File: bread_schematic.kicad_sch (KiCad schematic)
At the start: 1 part, among them U1 NHD-C0220BIZ

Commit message: xganges
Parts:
- removed U1: NHD-C0220BIZ, Display:NHD-C0220BiZ, symbol Display_Character:NHD-C0220BIZ
- added J1: Conn_01x04_Pin, symbol Connector:Conn_01x04_Pin
- added M1: ~, symbol _custom:NUCLEO_G031K8_CN3
- added M2: ~, symbol _custom:NUCLEO-G031K8_CN4
- added U2: TCS34725, TCS34725FN:SON65P200X240X70-6N, symbol TCS34725FN:TCS34725FN

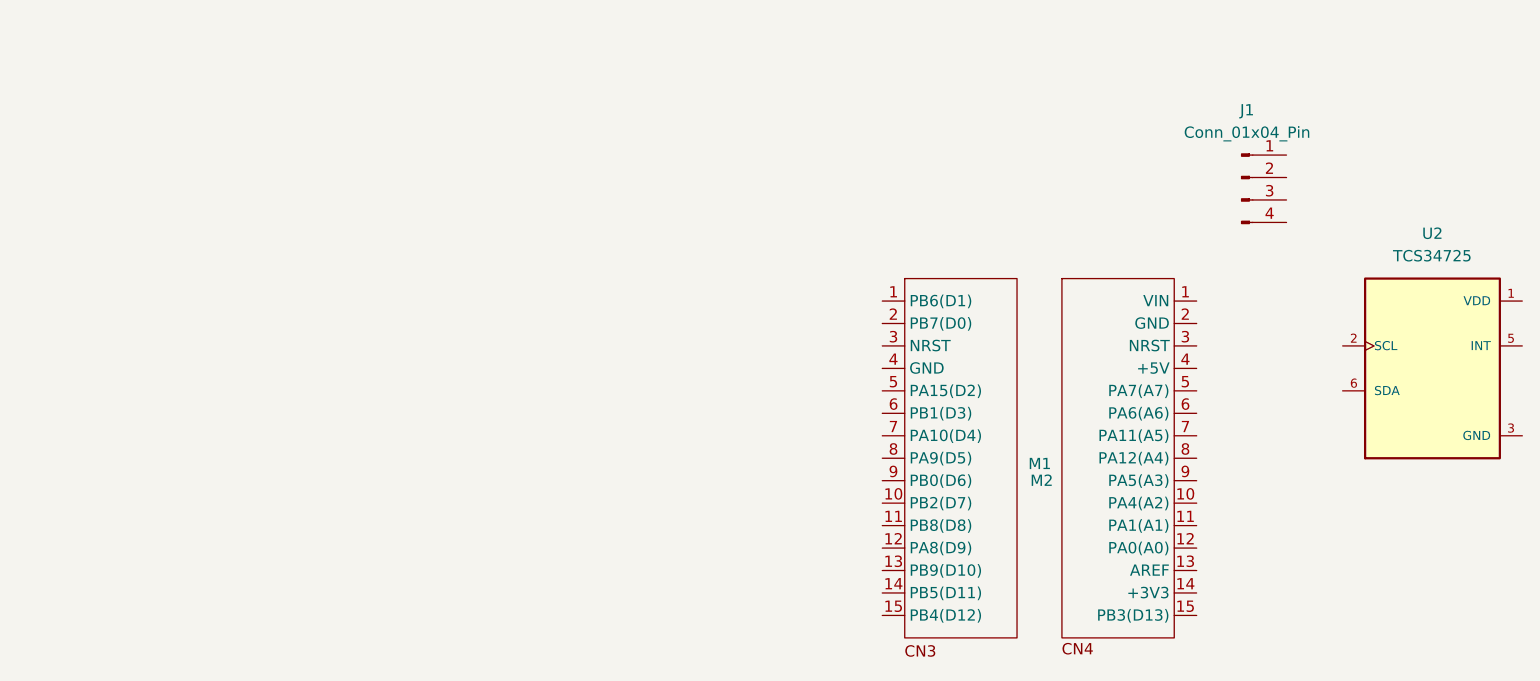
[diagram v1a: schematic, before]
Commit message: finished breadboard schematic
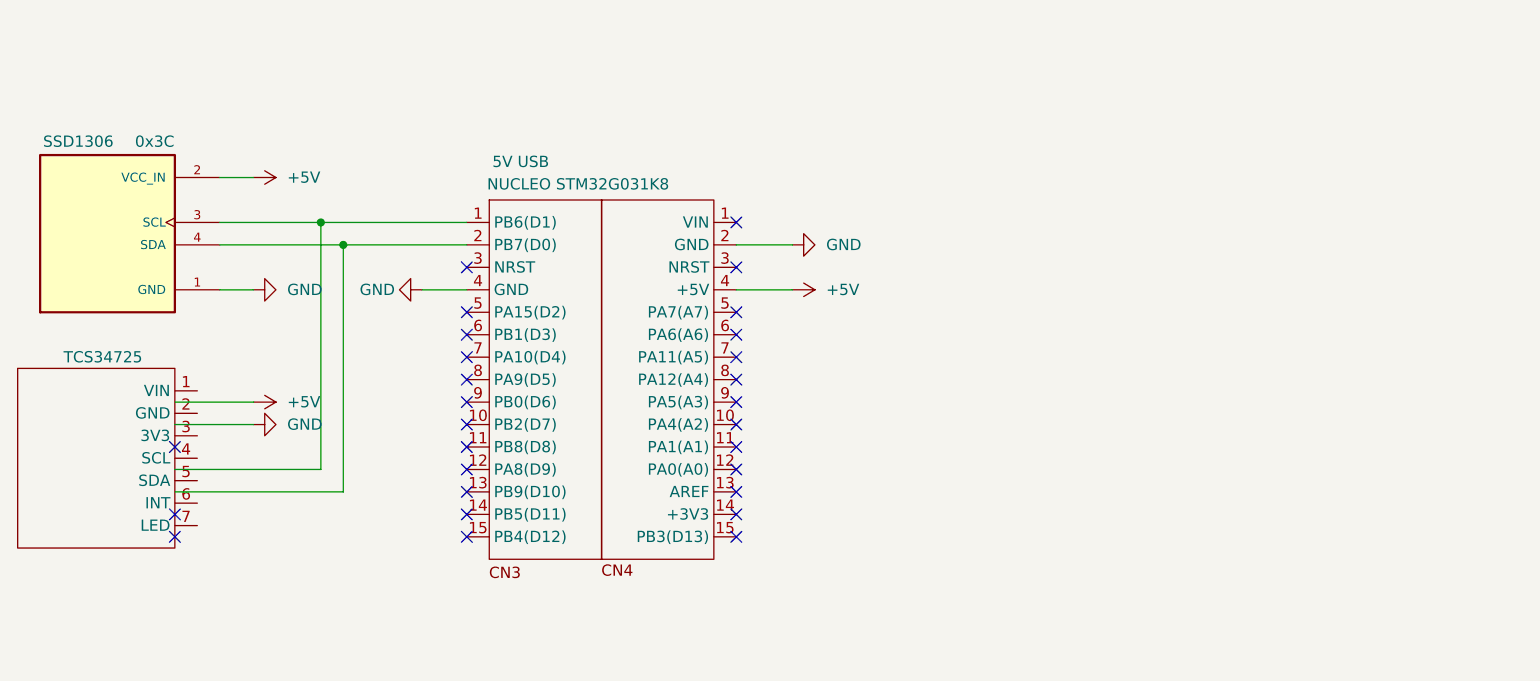
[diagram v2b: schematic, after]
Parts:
- removed J1: Conn_01x04_Pin, symbol Connector:Conn_01x04_Pin
- removed U2: TCS34725, TCS34725FN:SON65P200X240X70-6N, symbol TCS34725FN:TCS34725FN
- added U1: SSD1306, DM-OLED096-636:MODULE_DM-OLED096-636, symbol DM-OLED096-636:DM-OLED096-636
- added U2: TCS34725, symbol TCS34725:TCS34725
- M1: value ~ -> NUCLEO STM32G031K8
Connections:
- net at M1.1 (PB6(D1)): now also U1.3 (SCL)
- net at M1.2 (PB7(D0)): now also U1.4 (SDA)
- net GND: now reaches M1.4 (GND)
- net GND: now also M2.2 (GND), U1.1 (GND)
- net +5V: now reaches M2.4 (+5V)
- net +5V: now also U1.2 (VCC_IN)
- no-connect marks 0 -> 28
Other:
- company: (none) -> Jaedyn Carbonell
- title: (none) -> RGB Reader

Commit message: Update bread_schematic.kicad_sch
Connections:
- net +5V: now also U2.1 (VIN)
- net GND: now also U2.2 (GND)
- net at U2.4 (SCL): now also M1.1 (PB6(D1)), U1.3 (SCL)
- net at U2.5 (SDA): now also M1.2 (PB7(D0)), U1.4 (SDA)
